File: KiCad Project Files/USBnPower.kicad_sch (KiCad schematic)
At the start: 11 parts, among them J1 SM04B, U3 XC6206PxxxMR, U4 PRTR5V0U2X

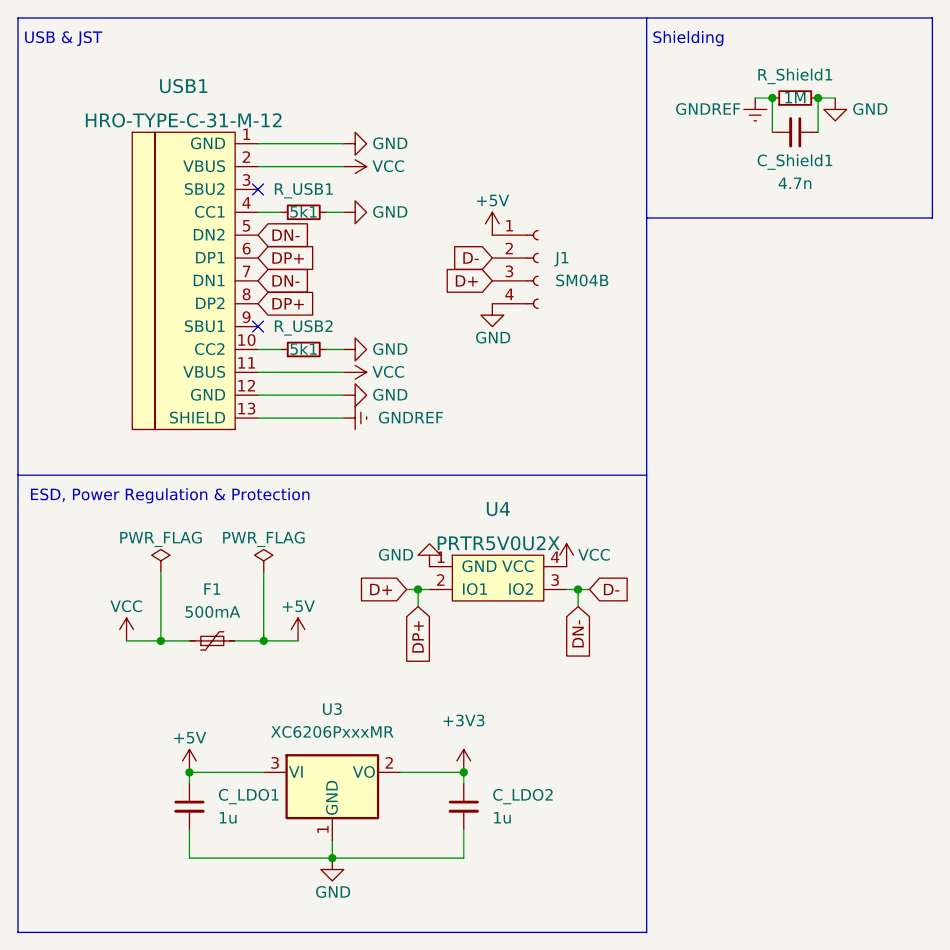
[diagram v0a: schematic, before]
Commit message: Add files via upload
updated schematics
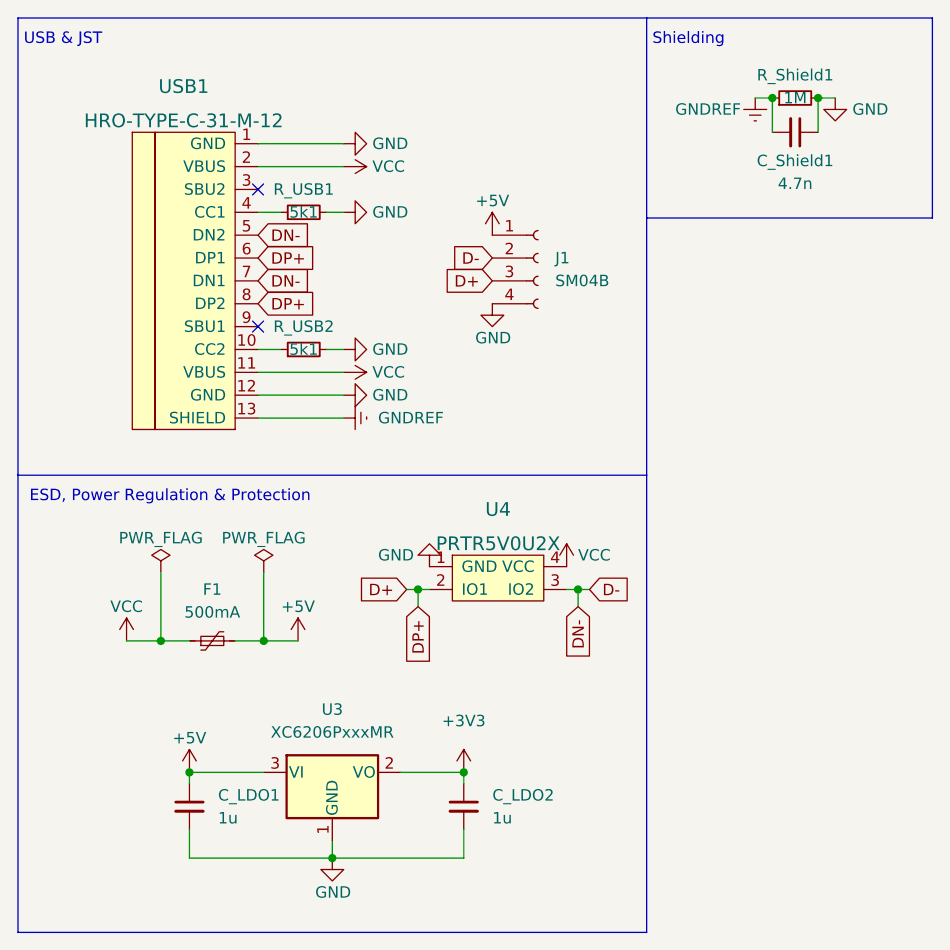
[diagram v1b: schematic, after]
